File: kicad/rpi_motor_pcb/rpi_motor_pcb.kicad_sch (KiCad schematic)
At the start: 15 parts, among them J1 Raspberry_Pi_2_3, J11 A-, J13 B-, J14 C-, J15 Y-, J16 Z-, J4 PWR IN, J8 X-, J9 LSW1

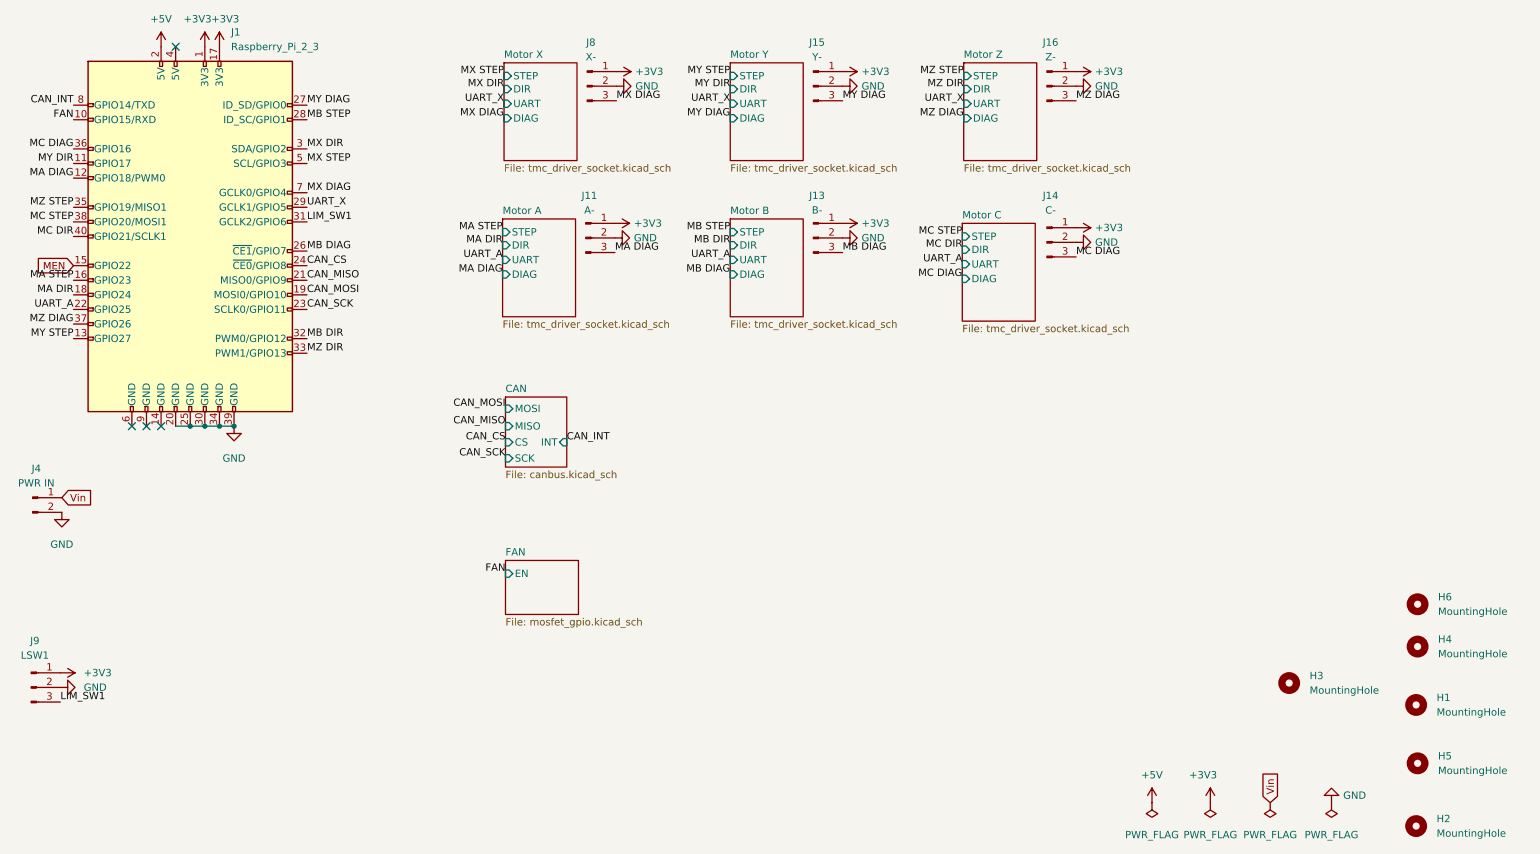
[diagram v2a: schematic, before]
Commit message: rpi_motor_pcb: 7-axis canbus version (removed useless fan and limit switch)
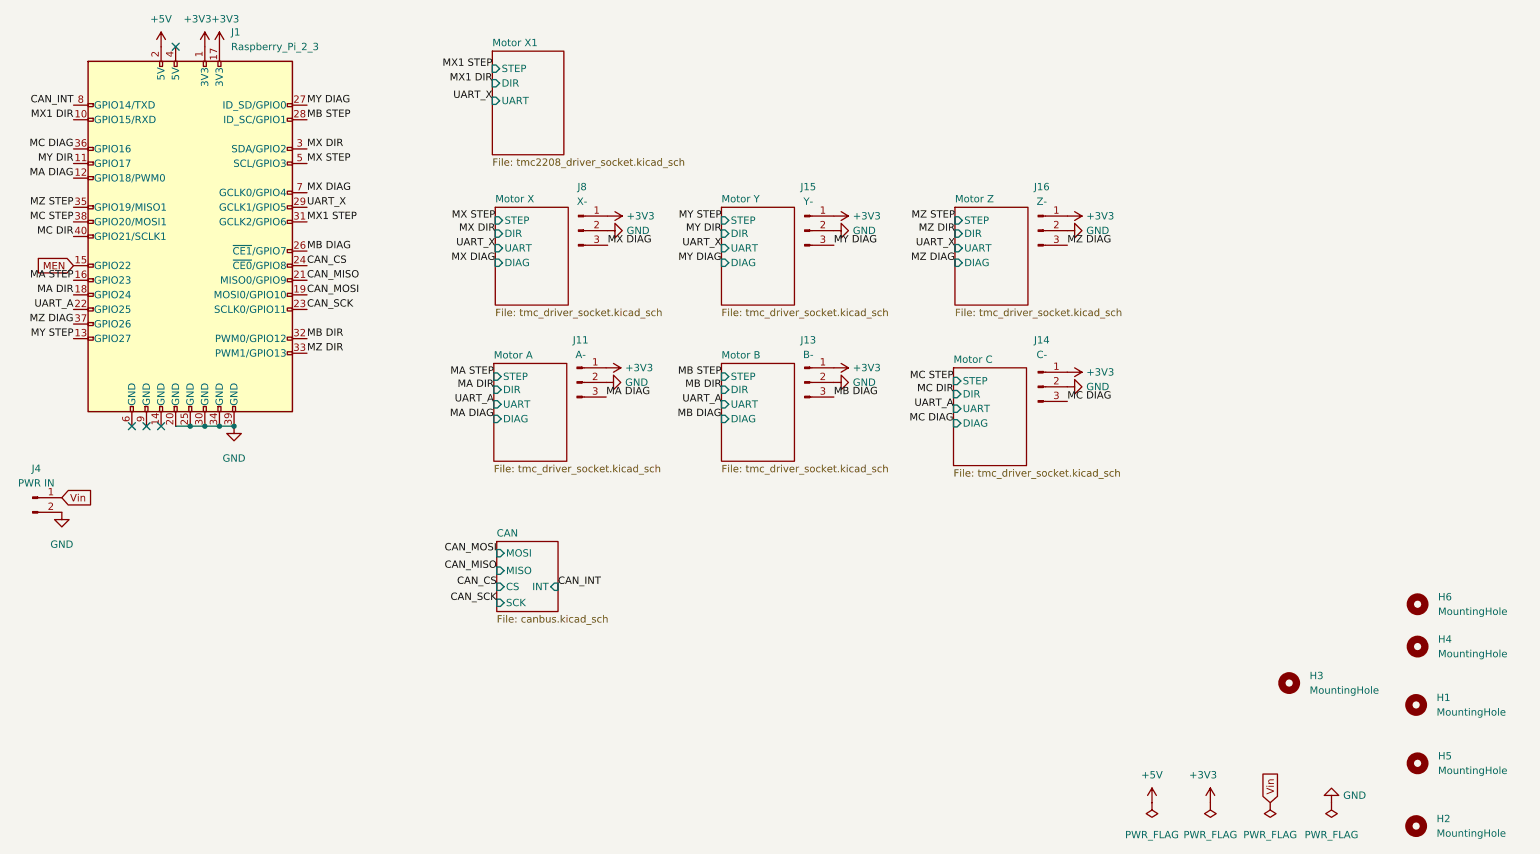
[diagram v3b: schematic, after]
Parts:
- removed J9: LSW1, Connector_JST:JST_XH_B3B-XH-A_1x03_P2.50mm_Vertical, symbol Connector:Conn_01x03_Male
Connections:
- net FAN renamed MX1 DIR
- net LIM_SW1 renamed MX1 STEP
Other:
- removed sheet FAN
- added sheet Motor X1 (tmc2208_driver_socket.kicad_sch)
- moved on the sheet: J11, J13, J14, J15, J16, J8

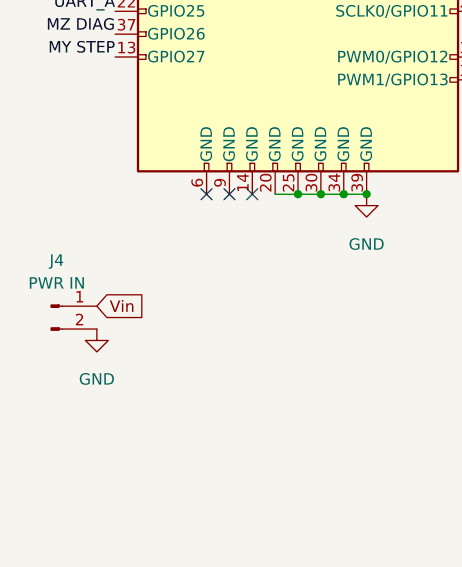
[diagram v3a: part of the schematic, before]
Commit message: rpi_motor_pcb: 6 axis version
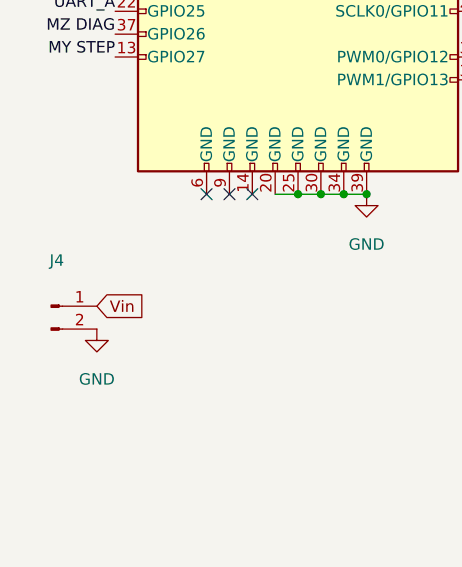
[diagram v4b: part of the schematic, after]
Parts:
- J4: value PWR IN -> (none); footprint Connector_JST:JST_XH_B2B-XH-A_1x02_P2.50mm_Vertical -> (none)
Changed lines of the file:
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@@
     (in_bom yes) (on_board yes) (fields_autoplaced)
     (property "Reference" "J4" (id 0) (at 19.685 93.218 0))
-    (property "Value" "PWR IN" (id 1) (at 19.685 95.758 0))
-    (property "Footprint" "Connector_JST:JST_XH_B2B-XH-A_1x02_P2.50mm_Vertical" (id 2) (at 19.05 98.298 0)
+    (property "Value" "" (id 1) (at 19.685 95.758 0))
+    (property "Footprint" "" (id 2) (at 19.05 98.298 0)
       (effects (font (size 1.27 1.27)) hide)
     )
@@
       (reference "#PWR03") (unit 1) (value "GND") (footprint "")
     )
+    (path "/6362900b-e28d-41f8-a76a-d9fd4cd7a7e6/1bc87082-5d9a-4e43-9e24-e7de0a9cf913"
+      (reference "#PWR04") (unit 1) (value "GND") (footprint "")
+    )
     (path "/2f97629b-ca35-40e1-950a-976dc6d5099e/7e0b5e6c-5e10-4bbc-b043-eb819dc2cf4f"
       (reference "#PWR05") (unit 1) (value "+3V3") (footprint "")
@@
       (reference "#PWR010") (unit 1) (value "GND") (footprint "")
     )
+    (path "/6362900b-e28d-41f8-a76a-d9fd4cd7a7e6/da957933-6555-482c-b9e9-870b7ba47d2d"
+      (reference "#PWR011") (unit 1) (value "GND") (footprint "")
+    )
     (path "/cbfe036f-5613-48df-a314-10875a3b599a/7e0b5e6c-5e10-4bbc-b043-eb819dc2cf4f"
       (reference "#PWR012") (unit 1) (value "+3V3") (footprint "")
@@
       (reference "#PWR015") (unit 1) (value "GND") (footprint "")
     )
+    (path "/6362900b-e28d-41f8-a76a-d9fd4cd7a7e6/c795ffae-7bba-4818-876a-0977b9f0ce69"
+      (reference "#PWR016") (unit 1) (value "GND") (footprint "")
+    )
     (path "/21d5a0dd-8380-4cbc-877d-09f4ecd37e4d/7e0b5e6c-5e10-4bbc-b043-eb819dc2cf4f"
       (reference "#PWR017") (unit 1) (value "+3V3") (footprint "")
@@
       (reference "#PWR020") (unit 1) (value "GND") (footprint "")
     )
+    (path "/6362900b-e28d-41f8-a76a-d9fd4cd7a7e6/2e88a8fb-fadc-4d43-9722-eb2aabe3081a"
+      (reference "#PWR021") (unit 1) (value "+3V3") (footprint "")
+    )
     (path "/19bc01f1-ddb0-42eb-b5a4-99228b6f4f71/7e0b5e6c-5e10-4bbc-b043-eb819dc2cf4f"
       (reference "#PWR022") (unit 1) (value "+3V3") (footprint "")
@@
       (reference "#PWR025") (unit 1) (value "GND") (footprint "")
     )
+    (path "/6362900b-e28d-41f8-a76a-d9fd4cd7a7e6/bd5f1000-a605-4da0-b543-4a7085ff9898"
+      (reference "#PWR026") (unit 1) (value "+3V3") (footprint "")
+    )
     (path "/11aba65b-53a2-477d-9cee-8bb1f5f76453/7e0b5e6c-5e10-4bbc-b043-eb819dc2cf4f"
       (reference "#PWR027") (unit 1) (value "+3V3") (footprint "")
@@
       (reference "#PWR070") (unit 1) (value "+3V3") (footprint "")
     )
+    (path "/6362900b-e28d-41f8-a76a-d9fd4cd7a7e6/10cf16a7-cc9e-4bef-a722-b4590b2aa0f9"
+      (reference "#PWR071") (unit 1) (value "+3V3") (footprint "")
+    )
     (path "/6c8d4f7f-654b-449c-86d5-a37fdd5ef321"
       (reference "#PWR072") (unit 1) (value "GND") (footprint "")
@@
       (reference "#PWR079") (unit 1) (value "GND") (footprint "")
     )
+    (path "/6362900b-e28d-41f8-a76a-d9fd4cd7a7e6/3df40294-f5be-41fd-8275-710435cb59b7"
+      (reference "#PWR080") (unit 1) (value "+3V3") (footprint "")
+    )
+    (path "/6362900b-e28d-41f8-a76a-d9fd4cd7a7e6/c48bf6db-6418-4875-959b-4af64220405a"
+      (reference "#PWR081") (unit 1) (value "GND") (footprint "")
+    )
+    (path "/6362900b-e28d-41f8-a76a-d9fd4cd7a7e6/b802db5a-fcc9-4d2b-9deb-83b5b5f1469d"
+      (reference "#PWR082") (unit 1) (value "GND") (footprint "")
+    )
     (path "/cefcb18b-530f-4319-8028-c078728148bf/e97943f2-ac8d-4bb9-b997-3b6fb46c2c40"
       (reference "#PWR083") (unit 1) (value "+3V3") (footprint "")
@@
       (reference "#PWR092") (unit 1) (value "GND") (footprint "")
     )
+    (path "/6362900b-e28d-41f8-a76a-d9fd4cd7a7e6/536ca051-0b0d-4742-8e8b-b24e32848138"
+      (reference "#PWR093") (unit 1) (value "GND") (footprint "")
+    )
     (path "/d020a2f5-1049-4c55-9a6f-82477ab73207"
       (reference "#PWR0101") (unit 1) (value "GND") (footprint "")
@@
       (reference "#PWR0124") (unit 1) (value "GND") (footprint "")
     )
-    (path "/6362900b-e28d-41f8-a76a-d9fd4cd7a7e6/10cf16a7-cc9e-4bef-a722-b4590b2aa0f9"
-      (reference "#PWR?") (unit 1) (value "+3V3") (footprint "")
-    )
-    (path "/6362900b-e28d-41f8-a76a-d9fd4cd7a7e6/1bc87082-5d9a-4e43-9e24-e7de0a9cf913"
-      (reference "#PWR?") (unit 1) (value "GND") (footprint "")
-    )
-    (path "/6362900b-e28d-41f8-a76a-d9fd4cd7a7e6/2e88a8fb-fadc-4d43-9722-eb2aabe3081a"
-      (reference "#PWR?") (unit 1) (value "+3V3") (footprint "")
-    )
-    (path "/6362900b-e28d-41f8-a76a-d9fd4cd7a7e6/3df40294-f5be-41fd-8275-710435cb59b7"
-      (reference "#PWR?") (unit 1) (value "+3V3") (footprint "")
-    )
-    (path "/6362900b-e28d-41f8-a76a-d9fd4cd7a7e6/536ca051-0b0d-4742-8e8b-b24e32848138"
-      (reference "#PWR?") (unit 1) (value "GND") (footprint "")
-    )
-    (path "/6362900b-e28d-41f8-a76a-d9fd4cd7a7e6/b802db5a-fcc9-4d2b-9deb-83b5b5f1469d"
-      (reference "#PWR?") (unit 1) (value "GND") (footprint "")
-    )
-    (path "/6362900b-e28d-41f8-a76a-d9fd4cd7a7e6/bd5f1000-a605-4da0-b543-4a7085ff9898"
-      (reference "#PWR?") (unit 1) (value "+3V3") (footprint "")
-    )
-    (path "/6362900b-e28d-41f8-a76a-d9fd4cd7a7e6/c48bf6db-6418-4875-959b-4af64220405a"
-      (reference "#PWR?") (unit 1) (value "GND") (footprint "")
-    )
-    (path "/6362900b-e28d-41f8-a76a-d9fd4cd7a7e6/c795ffae-7bba-4818-876a-0977b9f0ce69"
-      (reference "#PWR?") (unit 1) (value "GND") (footprint "")
-    )
-    (path "/6362900b-e28d-41f8-a76a-d9fd4cd7a7e6/da957933-6555-482c-b9e9-870b7ba47d2d"
-      (reference "#PWR?") (unit 1) (value "GND") (footprint "")
-    )
     (path "/1c9edd80-85d9-4c0d-9cc6-2c3a113885ca/29c05aa4-d4e2-4af1-a60e-827ca668e338"
       (reference "A1") (unit 1) (value "${SHEETNAME} Driver") (footprint "TMCSockets:TMC220X")
@@
     )
     (path "/6362900b-e28d-41f8-a76a-d9fd4cd7a7e6/5bee1450-13e4-4bbd-9925-fce3451ea2b7"
-      (reference "A?") (unit 1) (value "${SHEETNAME} Driver") (footprint "TMCSockets:TMC2208")
+      (reference "A7") (unit 1) (value "${SHEETNAME} Driver") (footprint "TMCSockets:TMC2208")
     )
     (path "/1c9edd80-85d9-4c0d-9cc6-2c3a113885ca/e81a27d8-8637-4524-870a-4b523b84e211"
@@
     )
     (path "/6362900b-e28d-41f8-a76a-d9fd4cd7a7e6/f6315dcd-4e20-4745-9366-c1557f1acd82"
-      (reference "C?") (unit 1) (value "100µF 50V") (footprint "Capacitor_SMD:CP_Elec_6.3x7.7")
+      (reference "C10") (unit 1) (value "100µF 50V") (footprint "Capacitor_SMD:CP_Elec_6.3x7.7")
     )
     (path "/3f7285bc-3a75-4010-bebc-ff3e7d481253"
@@
     )
     (path "/9d6262dc-7448-4646-b173-6662abd0d2b6"
-      (reference "J4") (unit 1) (value "PWR IN") (footprint "Connector_JST:JST_XH_B2B-XH-A_1x02_P2.50mm_Vertical")
+      (reference "J4") (unit 1) (value "PWR IN") (footprint "Connector_Phoenix_MC:PhoenixContact_MC_1,5_2-G-3.5_1x02_P3.50mm_Horizontal")
     )
     (path "/1c9edd80-85d9-4c0d-9cc6-2c3a113885ca/f268893d-d27d-4643-8d48-d1ca2e4e5a32"
@@
       (reference "J8") (unit 1) (value "X-") (footprint "Connector_PinHeader_2.54mm:PinHeader_1x03_P2.54mm_Vertical")
     )
+    (path "/6362900b-e28d-41f8-a76a-d9fd4cd7a7e6/c4d70727-9cca-4caf-8076-6717dbe96d02"
+      (reference "J9") (unit 1) (value "${SHEETNAME}") (footprint "Connector_JST:JST_XH_B4B-XH-A_1x04_P2.50mm_Vertical")
+    )
     (path "/cefcb18b-530f-4319-8028-c078728148bf/88514ba3-3c33-4eef-8020-c02f58bae04f"
       (reference "J10") (unit 1) (value "CAN") (footprint "Connector_JST:JST_XH_B2B-XH-A_1x02_P2.50mm_Vertical")
@@
       (reference "J16") (unit 1) (value "Z-") (footprint "Connector_PinHeader_2.54mm:PinHeader_1x03_P2.54mm_Vertical")
     )
-    (path "/6362900b-e28d-41f8-a76a-d9fd4cd7a7e6/c4d70727-9cca-4caf-8076-6717dbe96d02"
-      (reference "J?") (unit 1) (value "${SHEETNAME}") (footprint "Connector_JST:JST_XH_B4B-XH-A_1x04_P2.50mm_Vertical")
-    )
     (path "/1c9edd80-85d9-4c0d-9cc6-2c3a113885ca/a006615d-32f1-4530-8f68-5161c2fe10b0"
       (reference "JP1") (unit 1) (value "MS3") (footprint "Jumper:SolderJumper-3_P1.3mm_Open_RoundedPad1.0x1.5mm")
@@
     )
     (path "/6362900b-e28d-41f8-a76a-d9fd4cd7a7e6/2b99be8f-0e7b-4e16-b0ab-6cd851a45633"
-      (reference "JP?") (unit 1) (value "MS3") (footprint "Jumper:SolderJumper-3_P1.3mm_Open_RoundedPad1.0x1.5mm")
+      (reference "JP19") (unit 1) (value "MS3") (footprint "Jumper:SolderJumper-3_P1.3mm_Open_RoundedPad1.0x1.5mm")
+    )
+    (path "/6362900b-e28d-41f8-a76a-d9fd4cd7a7e6/d492d0db-fb4b-4b26-a22c-07acd77b2813"
+      (reference "JP20") (unit 1) (value "MS2") (footprint "Jumper:SolderJumper-3_P1.3mm_Open_RoundedPad1.0x1.5mm")
     )
     (path "/6362900b-e28d-41f8-a76a-d9fd4cd7a7e6/bce6dad0-f8bf-4037-a62e-5b1bec09552e"
-      (reference "JP?") (unit 1) (value "MS1") (footprint "Jumper:SolderJumper-3_P1.3mm_Open_RoundedPad1.0x1.5mm")
-    )
-    (path "/6362900b-e28d-41f8-a76a-d9fd4cd7a7e6/d492d0db-fb4b-4b26-a22c-07acd77b2813"
-      (reference "JP?") (unit 1) (value "MS2") (footprint "Jumper:SolderJumper-3_P1.3mm_Open_RoundedPad1.0x1.5mm")
+      (reference "JP21") (unit 1) (value "MS1") (footprint "Jumper:SolderJumper-3_P1.3mm_Open_RoundedPad1.0x1.5mm")
     )
     (path "/cefcb18b-530f-4319-8028-c078728148bf/2a32bb24-9b28-499a-b7ac-f9a5a80f0cad"
